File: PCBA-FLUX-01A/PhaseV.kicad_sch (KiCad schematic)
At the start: 60 parts, among them Q10 IPT015N10N5, Q11 BC817, Q7 IPT015N10N5, Q8 IPT015N10N5, Q9 IPT015N10N5, U5 INA240A2DR, U6 UCC27211AQDDARQ1, U7 TLV9001

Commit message: Changes were made
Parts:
- added C105: C, Capacitor_THT:C_Rect_L9.0mm_W6.4mm_P7.50mm_MKT, symbol Device:C
- added C96: 10nF, Capacitor_SMD:C_0603_1608Metric, symbol Device:C
- added R80, R81, R82, R83: 10R, Resistor_SMD:R_0805_2012Metric, symbol Device:R
- added R91: R, Resistor_SMD:R_1218_3246Metric, symbol Device:R
- R26, R27, R28, R42: footprint Resistor_SMD:R_0805_2012Metric -> Resistor_SMD:R_0603_1608Metric
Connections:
- net GND: now also C105.2
- net phV_Shunt+: now also R80.1, R81.1; no longer U5.8 (IN+)
- net phV_Shunt-: now also R82.1, R83.1; no longer U5.1 (IN-)
- net at C59.2, C60.2, Q10.3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: now also R91.1
- new net: C96.1, R80.2, R81.2, U5.8 (IN+)
- new net: C105.1, R91.2
- new net: C96.2, R82.2, R83.2, U5.1 (IN-)
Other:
- moved on the sheet: C53, C54, C55, C56, C57, C59, C60, D6, D7, D8, D9, Q10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

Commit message: Finished schematic?
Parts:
- removed C65, C67, C69, C72: 100nF, Capacitor_SMD:C_0805_2012Metric, symbol Device:C
- removed C66, C68, C71: 2.2uF, Capacitor_SMD:C_1210_3225Metric, symbol Device:C
- removed C70: 100nF, Capacitor_SMD:C_0402_1005Metric, symbol Device:C
- removed Q10: IPT015N10N5, Package_TO_SOT_SMD:Infineon_PG-HSOF-8-1_ThermalVias, symbol Bvrny's_library:IPT015N10N5
- removed Q11: BC817, Package_TO_SOT_SMD:SOT-23, symbol Transistor_BJT:BC817
- removed R44: 10k, Resistor_SMD:R_1206_3216Metric, symbol Device:R
- removed R45: 0.1mR, Bvrny's_library:R5930, symbol Device:R_Shunt
- removed R49: 2K2, Resistor_SMD:R_0603_1608Metric, symbol Device:R
- removed R50: 10K, Resistor_SMD:R_0603_1608Metric, symbol Device:R
- removed U5: INA240A2DR, Package_SO:SOIC-8_3.9x4.9mm_P1.27mm, symbol Bvrny's_library:INA240A2DR
- removed U6: UCC27211AQDDARQ1, Package_SO:SOIC-8-1EP_3.9x4.9mm_P1.27mm_EP2.95x4.9mm_Mask2.34x2.34mm_ThermalVias, symbol Bvrny's_library:UCC27211AQDDARQ1
- added C118, C120, C122, C124, C126: 1000uF, Capacitor_THT:CP_Radial_D18.0mm_P7.50mm, symbol Device:C_Polarized
- added C119, C121, C123, C125, C127: 10uF, Capacitor_SMD:C_1210_3225Metric, symbol Device:C
- added C128: 100nF, Capacitor_SMD:C_0805_2012Metric, symbol Device:C
- added C42, C46: 22uF, Capacitor_SMD:C_1206_3216Metric, symbol Device:C
- added C44, C49: 100nF, Capacitor_SMD:C_0402_1005Metric, symbol Device:C
- added Q19: BC860C, Package_TO_SOT_SMD:SOT-23, symbol Simulation_SPICE:PNP
- added Q6: IPT015N10N5, Package_TO_SOT_SMD:Infineon_PG-HSOF-8-1_ThermalVias, symbol Bvrny's_library:IPT015N10N5
- added R24: 100R, Resistor_SMD:R_0603_1608Metric, symbol Device:R
- added R44: 0.1mR, Bvrny's_library:R5930, symbol Device:R_Shunt
- added R45: 2K2, Resistor_SMD:R_0603_1608Metric, symbol Device:R
- added R94: 18k, Resistor_SMD:R_0603_1608Metric, symbol Synapse:R
- added U5: UCC27211AQDDARQ1, Package_SO:SOIC-8-1EP_3.9x4.9mm_P1.27mm_EP2.95x4.9mm_Mask2.34x2.34mm_ThermalVias, symbol Bvrny's_library:UCC27211AQDDARQ1
- added U6: INA240A2DR, Package_SO:SOIC-8_3.9x4.9mm_P1.27mm, symbol Bvrny's_library:INA240A2DR
- C51, C52: value 100nF -> 1nF; footprint Capacitor_SMD:C_0402_1005Metric -> Capacitor_SMD:C_0603_1608Metric; JLCPCB Part # C307331 -> C1588; JLCPCB price https://jlcpcb.com/partdetail/291005-CL05B104KB54PNC/C307331 -> https://jlcpcb.com/partdetail/1940-CL10B102KB8NNNC/C1588; MFR.Part # CL05B104KB54PNC -> CL10B102KB8NNNC; Package 0402 -> 0603
- C53: value 22uF -> 100nF; footprint Capacitor_SMD:C_1206_3216Metric -> Capacitor_SMD:C_0402_1005Metric; Dielectric X5R -> X7R; JLCPCB Part # C12891 -> C307331; JLCPCB price https://jlcpcb.com/partdetail/13537-CL31A226KAHNNNE/C12891 -> https://jlcpcb.com/partdetail/291005-CL05B104KB54PNC/C307331; MFR.Part # CL31A226KAHNNNE -> CL05B104KB54PNC; Package 1206 -> 0402; Voltage 25V -> 50V
- C54: value 22uF -> 2.2uF; Dielectric X5R -> X7R; JLCPCB Part # C12891 -> C50254; JLCPCB price https://jlcpcb.com/partdetail/13537-CL31A226KAHNNNE/C12891 -> https://jlcpcb.com/partdetail/51263-CL31B225KBHNNNE/C50254; MFR.Part # CL31A226KAHNNNE -> CL31B225KBHNNNE; Voltage 25V -> 50V
- C55: value 1nF -> 2.2nF; JLCPCB Part # C1588 -> C1604; JLCPCB price https://jlcpcb.com/partdetail/1940-CL10B102KB8NNNC/C1588 -> https://jlcpcb.com/partdetail/1956-0603B222K500NT/C1604; MFR.Part # CL10B102KB8NNNC -> 0603B222K500NT; Manufacturer Samsung Electro-Mechanics -> FH (Guangdong Fenghua Advanced Tech)
- C56: value 1nF -> 100nF; footprint Capacitor_SMD:C_0603_1608Metric -> Capacitor_SMD:C_0402_1005Metric; JLCPCB Part # C1588 -> C307331; JLCPCB price https://jlcpcb.com/partdetail/1940-CL10B102KB8NNNC/C1588 -> https://jlcpcb.com/partdetail/291005-CL05B104KB54PNC/C307331; MFR.Part # CL10B102KB8NNNC -> CL05B104KB54PNC; Package 0603 -> 0402
- C57: value 100nF -> 3.3nF; footprint Capacitor_SMD:C_0402_1005Metric -> Capacitor_SMD:C_0603_1608Metric; JLCPCB Part # C307331 -> C1613; JLCPCB price https://jlcpcb.com/partdetail/291005-CL05B104KB54PNC/C307331 -> https://jlcpcb.com/partdetail/1965-CL10B332KB8NNNC/C1613; MFR.Part # CL05B104KB54PNC -> CL10B332KB8NNNC; Manufacturer Samsung Electro-Mechanics -> Samsung Electro-Mechanics; Package 0402 -> 0603
- C58: value 2.2nF -> 100nF; footprint Capacitor_SMD:C_0603_1608Metric -> Capacitor_SMD:C_0402_1005Metric; JLCPCB Part # C1604 -> C307331; JLCPCB price https://jlcpcb.com/partdetail/1956-0603B222K500NT/C1604 -> https://jlcpcb.com/partdetail/291005-CL05B104KB54PNC/C307331; MFR.Part # 0603B222K500NT -> CL05B104KB54PNC; Manufacturer FH (Guangdong Fenghua Advanced Tech) -> Samsung Electro-Mechanics; Package 0603 -> 0402
- C59: value 2.2uF -> 1nF; footprint Capacitor_SMD:C_1206_3216Metric -> Capacitor_SMD:C_0603_1608Metric; JLCPCB Part # C50254 -> C1588; JLCPCB price https://jlcpcb.com/partdetail/51263-CL31B225KBHNNNE/C50254 -> https://jlcpcb.com/partdetail/1940-CL10B102KB8NNNC/C1588; MFR.Part # CL31B225KBHNNNE -> CL10B102KB8NNNC; Package 1206 -> 0603
- C60, C62: footprint Capacitor_SMD:C_0402_1005Metric -> Capacitor_SMD:C_0805_2012Metric; JLCPCB Part # C307331 -> C28233; JLCPCB price https://jlcpcb.com/partdetail/291005-CL05B104KB54PNC/C307331 -> https://jlcpcb.com/partdetail/28983-CL21B104KCFNNNE/C28233; MFR.Part # CL05B104KB54PNC -> CL21B104KCFNNNE; Package 0402 -> 0805; Voltage 50V -> 100V
- C61: value 3.3nF -> 100nF; footprint Capacitor_SMD:C_0603_1608Metric -> Capacitor_SMD:C_0805_2012Metric; JLCPCB Part # C1613 -> C28233; JLCPCB price https://jlcpcb.com/partdetail/1965-CL10B332KB8NNNC/C1613 -> https://jlcpcb.com/partdetail/28983-CL21B104KCFNNNE/C28233; MFR.Part # CL10B332KB8NNNC -> CL21B104KCFNNNE; Manufacturer Samsung Electro-Mechanics -> Samsung Electro-Mechanics; Package 0603 -> 0805; Voltage 50V -> 100V
- C63: value 1nF -> 100nF; footprint Capacitor_SMD:C_0603_1608Metric -> Capacitor_SMD:C_0402_1005Metric; JLCPCB Part # C1588 -> C307331; JLCPCB price https://jlcpcb.com/partdetail/1940-CL10B102KB8NNNC/C1588 -> https://jlcpcb.com/partdetail/291005-CL05B104KB54PNC/C307331; MFR.Part # CL10B102KB8NNNC -> CL05B104KB54PNC; Package 0603 -> 0402; Voltage 50V -> (none); Voltage rating (none) -> 50V
- C64: value 2.2uF -> 100nF; footprint Capacitor_SMD:C_1210_3225Metric -> Capacitor_SMD:C_0805_2012Metric; JLCPCB Part # C153036 -> C28233; JLCPCB price https://jlcpcb.com/partdetail/164378-FS32X225K101EGG/C153036 -> https://jlcpcb.com/partdetail/28983-CL21B104KCFNNNE/C28233; MFR.Part # FS32X225K101EGG -> CL21B104KCFNNNE; Manufacturer PSA(Prosperity Dielectrics) -> Samsung Electro-Mechanics; Package 1210 -> 0805
- R27: footprint Resistor_SMD:R_0603_1608Metric -> palmkiLib:R_0603_1608Metric
- R28: value 100R -> 1R; footprint Resistor_SMD:R_0603_1608Metric -> Resistor_SMD:R_1206_3216Metric; JLCPCB Part # C22775 -> C17928; JLCPCB price https://jlcpcb.com/partdetail/23502-0603WAF1000T5E/C22775 -> https://jlcpcb.com/partdetail/18616-1206W4F100KT5E/C17928; MFR.Part # 0603WAF1000T5E -> 1206W4F100KT5E; Package 0603 -> 1206
- R30, R39: value 1R -> 3R3; JLCPCB Part # C17928 -> C2783335; JLCPCB price https://jlcpcb.com/partdetail/18616-1206W4F100KT5E/C17928 -> https://jlcpcb.com/partdetail/2921791-NS06W4F330KT5E/C27833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; MFR.Part # 1206W4F100KT5E -> NS06W4F330KT5E
- R32, R41: value 3R3 -> 10k; JLCPCB Part # C2783335 -> C17902; JLCPCB price https://jlcpcb.com/partdetail/2921791-NS06W4F330KT5E/C27833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 -> https://jlcpcb.com/partdetail/18590-1206W4F1002T5E/C17902; MFR.Part # NS06W4F330KT5E -> 1206W4F1002T5E
- R34: value 10k -> 51k; footprint Resistor_SMD:R_1206_3216Metric -> Resistor_SMD:R_0805_2012Metric; JLCPCB Part # C17902 -> C17737; JLCPCB price https://jlcpcb.com/partdetail/18590-1206W4F1002T5E/C17902 -> https://jlcpcb.com/partdetail/18425-0805W8F5102T5E/C17737; MFR.Part # 1206W4F1002T5E -> 0805W8F5102T5E; Package 1206 -> 0805
- R36: value 51k -> 4k7; JLCPCB Part # C17737 -> C17673; JLCPCB price https://jlcpcb.com/partdetail/18425-0805W8F5102T5E/C17737 -> https://jlcpcb.com/partdetail/18361-0805W8F4701T5E/C17673; MFR.Part # 0805W8F5102T5E -> 0805W8F4701T5E
- R37: value 4k7 -> 1R; footprint Resistor_SMD:R_0805_2012Metric -> Resistor_SMD:R_1206_3216Metric; JLCPCB Part # C17673 -> C17928; JLCPCB price https://jlcpcb.com/partdetail/18361-0805W8F4701T5E/C17673 -> https://jlcpcb.com/partdetail/18616-1206W4F100KT5E/C17928; MFR.Part # 0805W8F4701T5E -> 1206W4F100KT5E; Package 0805 -> 1206
- R42: value 100R -> 10k; footprint Resistor_SMD:R_0603_1608Metric -> Resistor_SMD:R_1206_3216Metric; JLCPCB Part # C22775 -> C17902; JLCPCB price https://jlcpcb.com/partdetail/23502-0603WAF1000T5E/C22775 -> https://jlcpcb.com/partdetail/18590-1206W4F1002T5E/C17902; MFR.Part # 0603WAF1000T5E -> 1206W4F1002T5E; Package 0603 -> 1206
- R43: value 10k -> 100R; footprint Resistor_SMD:R_1206_3216Metric -> Resistor_SMD:R_0603_1608Metric; JLCPCB Part # C17902 -> C22775; JLCPCB price https://jlcpcb.com/partdetail/18590-1206W4F1002T5E/C17902 -> https://jlcpcb.com/partdetail/23502-0603WAF1000T5E/C22775; MFR.Part # 1206W4F1002T5E -> 0603WAF1000T5E; Package 1206 -> 0603
- R46: value 2K2 -> 560R; JLCPCB Part # C4190 -> C23204; JLCPCB price https://jlcpcb.com/partdetail/4597-0603WAF2201T5E/C4190 -> https://jlcpcb.com/partdetail/23931-0603WAF5600T5E/C23204; MFR.Part # 0603WAF2201T5E -> 0603WAF5600T5E
- R47: value 560R -> 0R; JLCPCB Part # C23204 -> C21189; JLCPCB price https://jlcpcb.com/partdetail/23931-0603WAF5600T5E/C23204 -> https://jlcpcb.com/partdetail/21903-0603WAF0000T5E/C21189; MFR.Part # 0603WAF5600T5E -> 0603WAF0000T5E
- R48: value 0R -> 10K; JLCPCB Part # C21189 -> C25804; JLCPCB price https://jlcpcb.com/partdetail/21903-0603WAF0000T5E/C21189 -> https://jlcpcb.com/partdetail/26547-0603WAF1002T5E/C25804; MFR.Part # 0603WAF0000T5E -> 0603WAF1002T5E
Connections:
- net +12V: now also C42.1, C46.1, U5.1 (VDD); no longer C54.1, C57.1
- net +3.3VA: now also C58.1, R47.1, C44.1, C49.1, Q19.3 (E), R94.1, U6.3 (REF2), U6.6 (VS); no longer C51.1, C52.1, C62.1, R48.1
- net +VSYS: now also C60.1, C61.1, C62.1, Q8.3, C118.1, C119.1, C120.1, C121.1, C122.1, C123.1, C124.1, C125.1, C126.1, C127.1, C128.1, Q6.3; no longer Q7.3, Q9.3
- net GND: now also C59.2, C60.2, Q7.2, Q9.2, R33.2, R36.2, R42.2, C118.2, C119.2, C120.2, C121.2, C122.2, C123.2, C124.2, C125.2, C126.2, C127.2, C128.2, C42.2, C44.2, C46.2, C49.2, U5.7 (VSS), U5.9 (Pad), U6.2 (GND), U6.4 (NC), U6.7 (REF1); no longer C54.2, C56.2, Q8.2, R34.2, R37.2
- net HSgate: now also R28.1, R30.1, R37.1, R39.1, U5.3 (HO); no longer R29.1, R31.1, R38.1, R40.1
- net LSgate: now also R29.1, R31.1, R38.1, R40.1, U5.8 (LO); no longer R30.1, R32.1, R39.1, R41.1
- net PhaseV_out: now also R34.1, R44.4; no longer R35.1
- net phV_HI: now also R24.1; no longer R26.1
- net phV_LO: now also R26.1; no longer R27.1
- net phV_NTCctrl: now also R45.1; no longer R46.1
- net phV_NTCout: now also C63.1, R48.2
- net phV_Shunt+: now also R44.2
- net phV_Shunt-: now also R44.3
- net phV_current: now also C55.1, R27.2; no longer C58.1, R28.2
- net phV_voltage: now also C59.1, R43.2; no longer C63.1, R42.2
- net at C96.1, R80.2, R81.2: now also U6.8 (IN+)
- net at R26.2: now also C52.1, U5.6 (LI); no longer C55.1
- net at C56.1: now also C54.1, U5.2 (HB); no longer R27.2
- net at R39.2: now also D8.2 (A), Q8.1, R41.1; no longer D9.1 (K)
- net at R41.2: now also C54.2, C56.2, Q7.3, Q8.2, Q9.3, R32.2, R91.1, Q6.2, R44.1, U5.4 (HS); no longer D9.2 (A)
- net at D6.1 (K): now also R28.2; no longer R29.2
- net at Q7.1, R31.2, R33.1: now also D7.2 (A); no longer D6.2 (A)
- net at Q9.1, R40.2: now also D9.2 (A), R42.1; no longer D8.2 (A), R43.1
- net at R30.2: now also D6.2 (A), R32.1, Q6.1; no longer D7.1 (K)
- net at R47.2: now also R46.1, Q19.1 (C); no longer TH2.1
- net at U7.1 (OUT), U7.4 (IN-): now also R43.1; no longer R42.1
- net at R46.2: now also R48.1, TH2.1, R94.2
- net at C96.2, R82.2, R83.2: now also U6.1 (IN-)
- net at R35.2, R36.1: now also C57.1, U7.3 (IN+)
- net at R38.2: now also D9.1 (K); no longer D8.1 (K)
- new net: C51.1, R24.2, U5.5 (HI)
- new net: Q19.2 (B), R45.2
- new net: R34.2, R35.1
- new net: D8.1 (K), R37.2
- new net: R27.1, U6.5 (OUT)
- new net: D7.1 (K), R29.2
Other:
- note added: "Current Sense"
- note added: "DC-Link"
- note added: "Gate driver & bridge"
- note added: "Phase Temp"
- note added: "Phase Voltage"

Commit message: Started with Flux layout
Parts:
- added C140, C141: 10uF, Capacitor_SMD:C_1210_3225Metric, symbol Device:C
- added C142: 100nF, Capacitor_SMD:C_0805_2012Metric, symbol Device:C
- R27: footprint palmkiLib:R_0603_1608Metric -> Resistor_SMD:R_0603_1608Metric
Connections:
- net +VSYS: now also C140.1, C141.1, C142.1
- net GND: now also C140.2, C141.2, C142.2

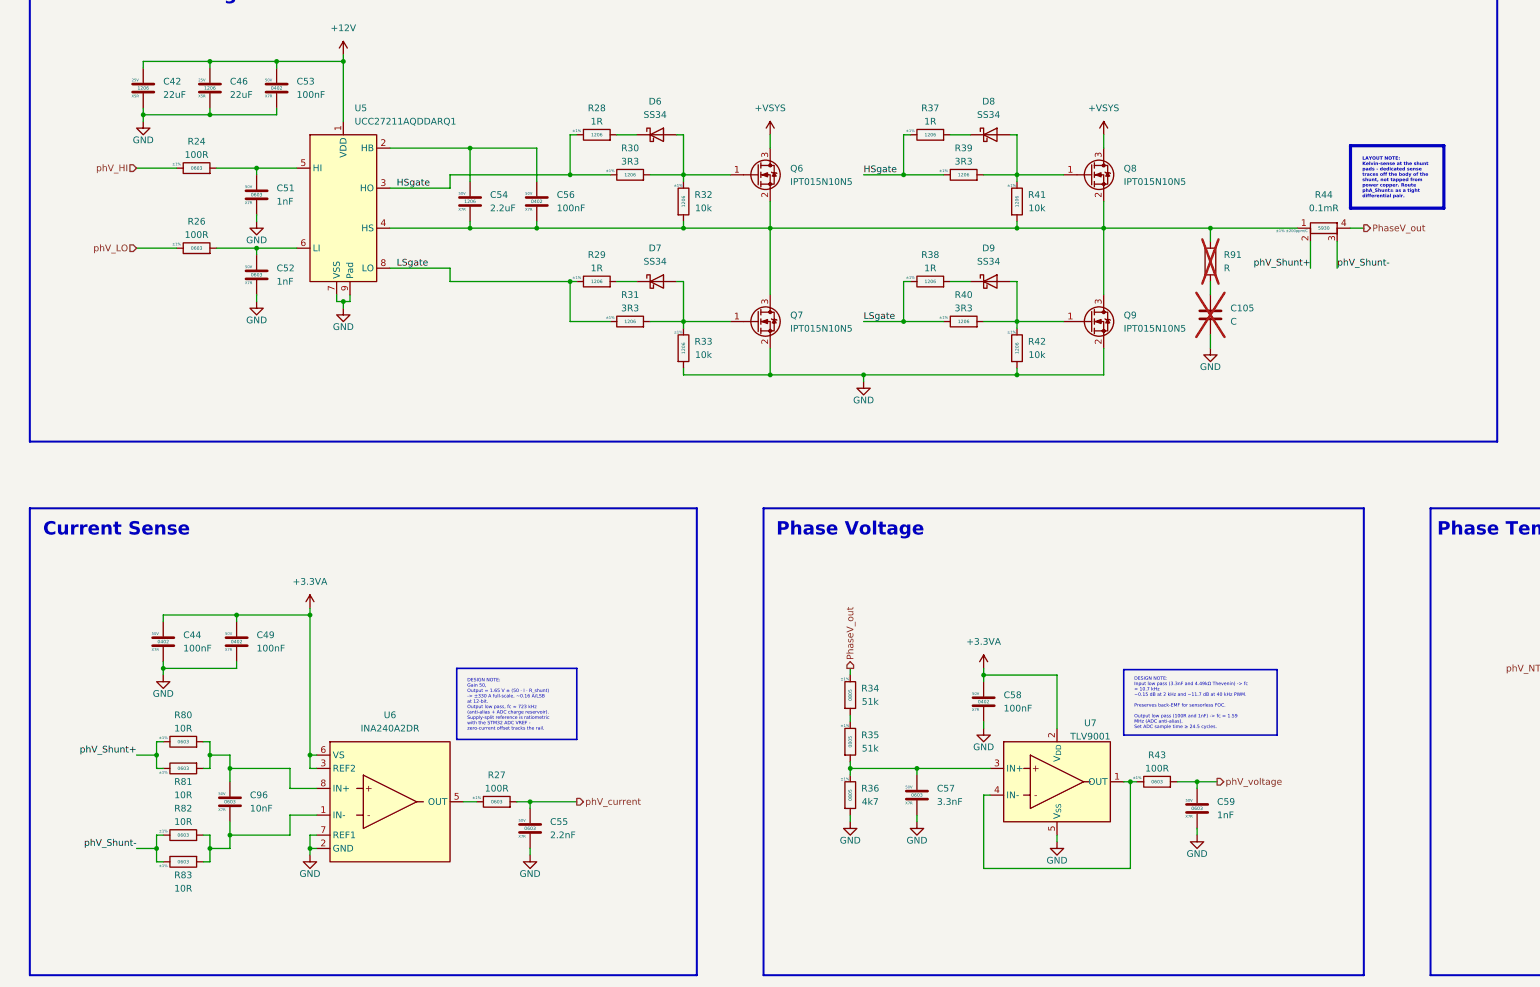
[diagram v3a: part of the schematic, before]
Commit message: Moved the current and voltage sensing OpAmp's to Vector
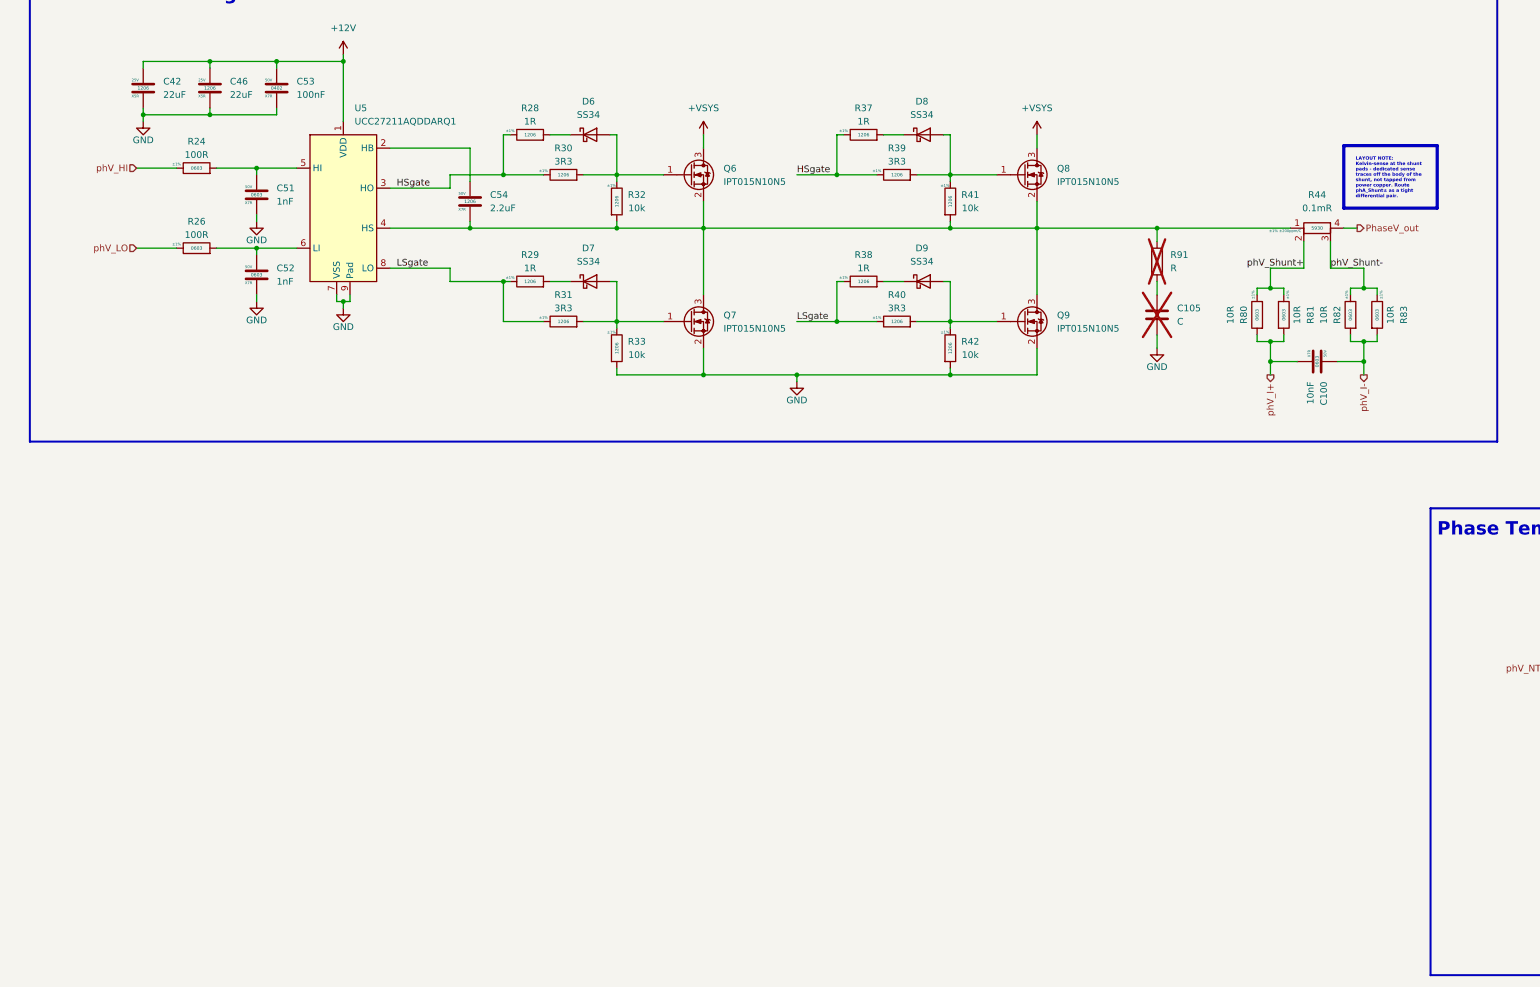
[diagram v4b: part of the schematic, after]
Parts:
- removed C44, C49, C56, C58: 100nF, Capacitor_SMD:C_0402_1005Metric, symbol Device:C
- removed C55: 2.2nF, Capacitor_SMD:C_0603_1608Metric, symbol Device:C
- removed C57: 3.3nF, Capacitor_SMD:C_0603_1608Metric, symbol Device:C
- removed C59: 1nF, Capacitor_SMD:C_0603_1608Metric, symbol Device:C
- removed C96: 10nF, Capacitor_SMD:C_0603_1608Metric, symbol Device:C
- removed R27, R43: 100R, Resistor_SMD:R_0603_1608Metric, symbol Device:R
- removed R34, R35: 51k, Resistor_SMD:R_0805_2012Metric, symbol Device:R
- removed R36: 4k7, Resistor_SMD:R_0805_2012Metric, symbol Device:R
- removed U6: INA240A2DR, Package_SO:SOIC-8_3.9x4.9mm_P1.27mm, symbol Bvrny's_library:INA240A2DR
- removed U7: TLV9001, Package_TO_SOT_SMD:SOT-23-5, symbol Bvrny's_library:TLV9001IDBVR
- added C100: 10nF, Capacitor_SMD:C_0603_1608Metric, symbol Device:C
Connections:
- net phV_I+: now reaches R80.2, R81.2
- net phV_I+: now also C100.2
- net phV_I-: now reaches R82.2, R83.2
- net phV_I-: now also C100.1
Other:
- note removed: "Current Sense"
- note removed: "Phase Voltage"
- moved on the sheet: C105, D6, D7, D8, D9, Q6, Q7, Q8, Q9, R28, R29, R30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
